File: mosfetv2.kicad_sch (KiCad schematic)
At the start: 26 parts

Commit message: thermal calculations done and Shunt Resistors changed. Not 3, just 2 resistors can dissipate the power.
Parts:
- removed Rsense_A?, Rsense_B?, Rsense_C?: 3mohm, CSNL2512FT3L00:RESC6331X75N, symbol CSNL2512FT3L00:CSNL2512FT3L00
- Rsense_A4: renamed from Rsense_A?; value 3mohm -> 2mohm; footprint CSNL2512FT3L00:RESC6331X75N -> CRF2512-FZ-R002ELF:RESC6432X80N
- Rsense_A5: renamed from Rsense_A?; value 3mohm -> 2mohm
- Rsense_B4, Rsense_B5: renamed from Rsense_B?; value 3mohm -> 2mohm; footprint CSNL2512FT3L00:RESC6331X75N -> CRF2512-FZ-R002ELF:RESC6432X80N
- Rsense_C4, Rsense_C5: renamed from Rsense_C?; value 3mohm -> 2mohm; footprint CSNL2512FT3L00:RESC6331X75N -> CRF2512-FZ-R002ELF:RESC6432X80N
- gave numbers to parts that had none: 17
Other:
- note added: "1.5"
- note added: "Bu değeri biraza daha düşürebiliriz thermal vialar ile"
- note added: "Daha yüksek akımlarla çalışabilmek için soğutma işini güçlendirmek gereklidir!"
- note added: "I = 20A RDSON = 0.005 OHM PLOSS = I^2 * R PLOSS = 2 W ----- RDSON(T=125) = 1.5*0.005 = 0.0075 OHM PLOSS = 3 W ----- MOSFET TEMPERATURE = 25 + 3 * 31.3 = 118.9 C"
- note added: "Sense resistor's power dissipation calculated as: Pmax = Imax^2 * R Pmax = 60^2 * 0.001 Pmax = 3.6 W. So We can use 2 2W resistors. Also we can not achive 60 Amps already."
- note added: "Sense resistor's voltage drop calculated as: Vs = Imax * R Vs = 60 * R (Imax from datasheet, 66A -> 60A) V_SOX: DRV8323 current sense output pin voltage Gain = 40 (Gain selected maximum bcs of power dissipation on shunt resistors) R = 0.001 OHM Vs = 60 * 0.001 = 0.060 V V_SOX = Vs * Gain (Gain = 5/10/20/40) V_SOX = 0.060 *40 = 2.4 V 2.4 V -> 60A -> 3000 (ADC raw) 3.3 V -> 82.5A -> 4095 (ADC raw) 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"
- note added: "Termal Hesaplamalar"
- note added: "WORKING CONDITIONS CONSIDERED AS: I = 20 A T = 120 C Because of thermal cooling limitations"
- note added: "f(I) = T y = I^2*0.0075*31.3+25 y = 0.23475 * I^2 + 25"
- note added: "https://jrainimo.com/build/2024/11/oss-thermal-simulation-of-pcbs/ Açık kaynaklı programları kullanarak sıcaklık analizi yapılabilir."

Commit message: Footprints prepared, first pcb project created.
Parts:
- C29, C31: footprint ul_80ZLJ680MGC18X25:CAP_YX_18X25_RUB -> ul_80ZLJ680MGC18X25:80ZLJ680MGC18X25
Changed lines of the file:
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@@
 			)
 		)
-		(property "Footprint" "ul_80ZLJ680MGC18X25:CAP_YX_18X25_RUB"
+		(property "Footprint" "ul_80ZLJ680MGC18X25:80ZLJ680MGC18X25"
 			(at 265.43 33.02 0)
 			(effects
@@
 			)
 		)
-		(property "Footprint" "ul_80ZLJ680MGC18X25:CAP_YX_18X25_RUB"
+		(property "Footprint" "ul_80ZLJ680MGC18X25:80ZLJ680MGC18X25"
 			(at 238.76 34.29 0)
 			(effects

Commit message: component list updated, all footprints updated and now they are compatible to produce with hand (no 0402 size)
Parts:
- Q10, Q11, Q12, Q8, Q9: footprint STL90N6F7 -> STL90N6F7:STL90N6F7
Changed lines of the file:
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@@
 			)
 		)
-		(property "Footprint" "STL90N6F7"
+		(property "Footprint" "STL90N6F7:STL90N6F7"
 			(at 166.37 186.36 0)
 			(effects
@@
 			)
 		)
-		(property "Footprint" "STL90N6F7"
+		(property "Footprint" "STL90N6F7:STL90N6F7"
 			(at 109.22 186.36 0)
 			(effects
@@
 			)
 		)
-		(property "Footprint" "STL90N6F7"
+		(property "Footprint" "STL90N6F7:STL90N6F7"
 			(at 224.79 186.36 0)
 			(effects
@@
 			)
 		)
-		(property "Footprint" "STL90N6F7"
+		(property "Footprint" "STL90N6F7:STL90N6F7"
 			(at 224.79 158.42 0)
 			(effects
@@
 			)
 		)
-		(property "Footprint" "STL90N6F7"
+		(property "Footprint" "STL90N6F7:STL90N6F7"
 			(at 166.37 158.42 0)
 			(effects

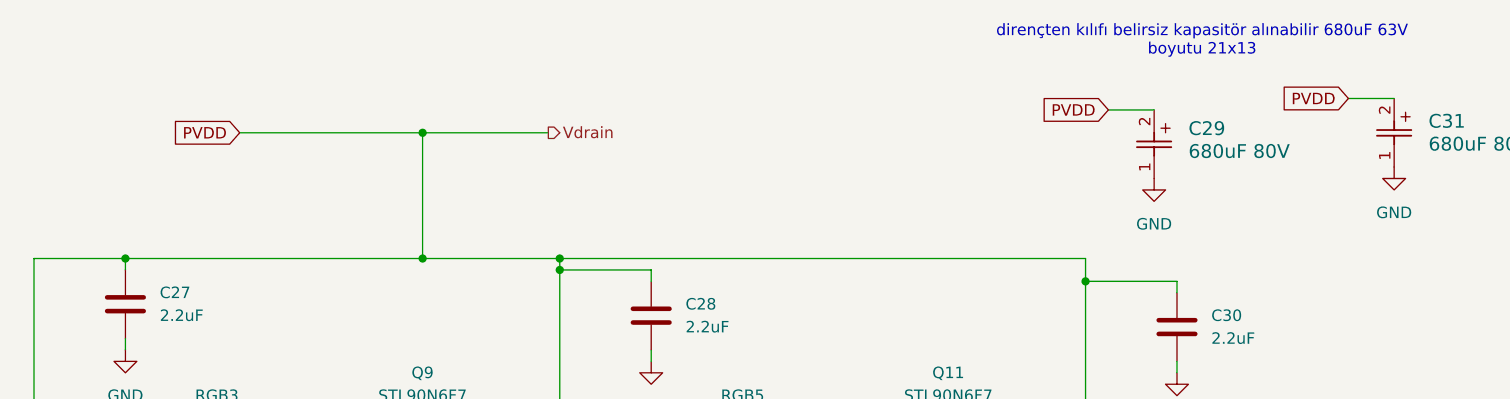
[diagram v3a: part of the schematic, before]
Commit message: some tags chaneged, pcb thinked about pcb component placement, aluminum mosfet carrier pcb and paralelling mosfets
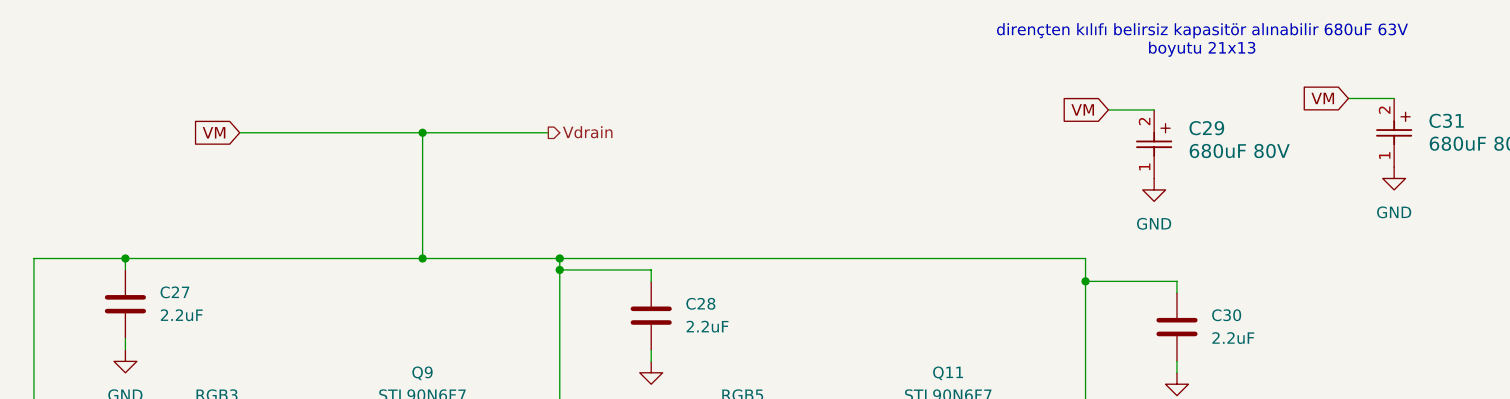
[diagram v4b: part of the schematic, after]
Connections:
- net PVDD renamed VM
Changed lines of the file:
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@@
 		)
 	)
-	(global_label "PVDD"
+	(global_label "VM"
 		(shape input)
 		(at 260.35 25.4 180)
@@
 		)
 	)
-	(global_label "PVDD"
+	(global_label "VM"
 		(shape input)
 		(at 233.68 26.67 180)
@@
 		)
 	)
-	(global_label "PVDD"
+	(global_label "VM"
 		(shape input)
 		(at 137.16 29.21 180)

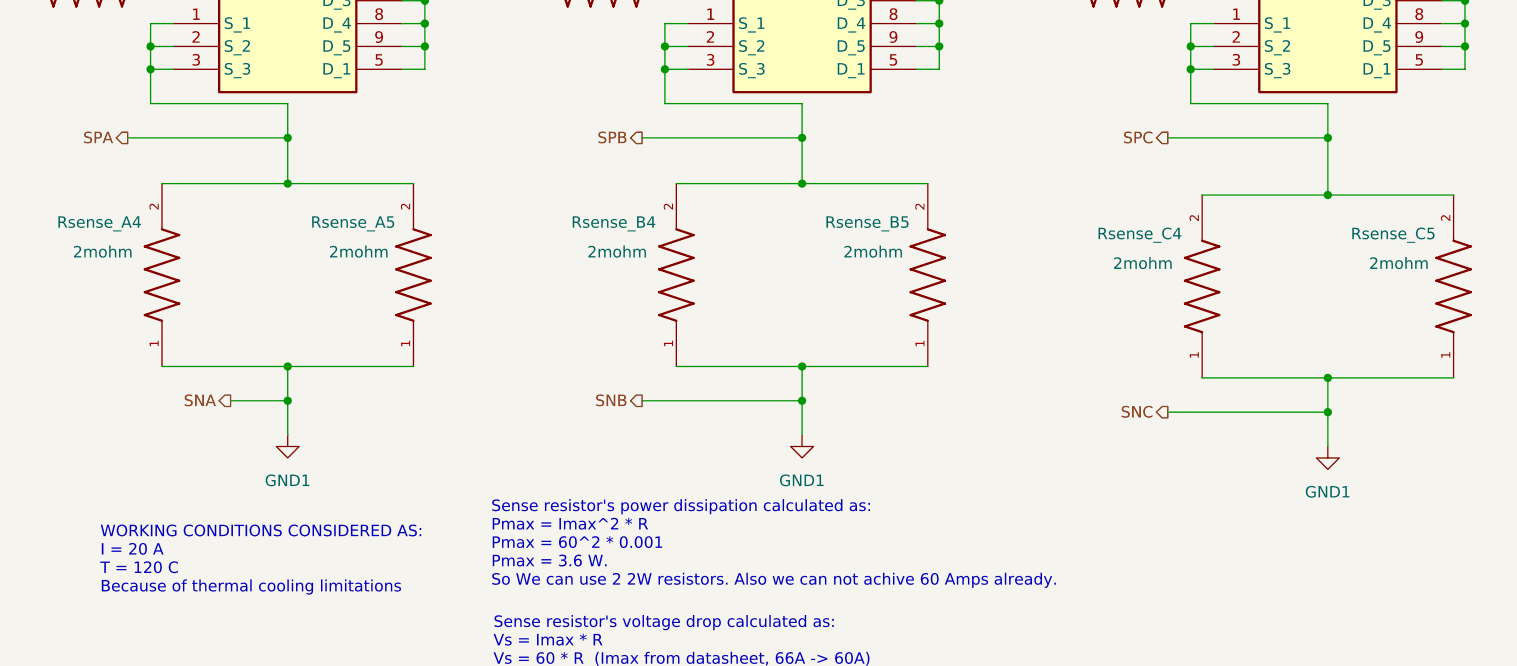
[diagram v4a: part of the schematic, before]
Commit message: started to pcb design, mosfets,shunts drv8323 placement.
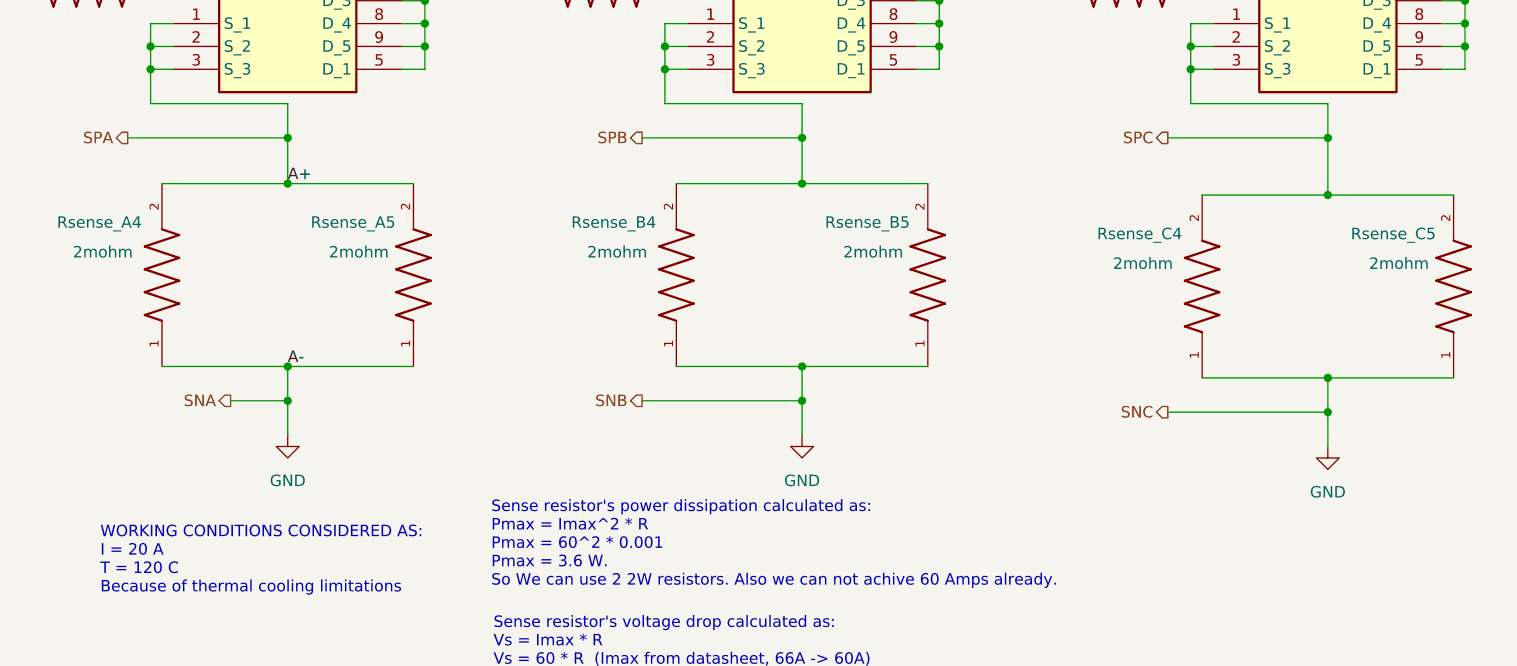
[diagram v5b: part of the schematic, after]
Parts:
- Rsense_A5: footprint CSNL2512FT3L00:RESC6331X75N -> CRF2512-FZ-R002ELF:RESC6432X80N
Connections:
- net GND1 is gone; now on net GND: Rsense_A4.1, Rsense_A5.1, Rsense_B4.1, Rsense_B5.1, Rsense_C4.1, Rsense_C5.1
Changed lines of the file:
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@@
 	(wire
 		(pts
+			(xy 100.33 114.3) (xy 86.36 114.3)
+		)
+		(stroke
+			(width 0)
+			(type default)
+		)
+	)
+	(wire
+		(pts
 			(xy 115.57 91.44) (xy 115.57 93.98)
 		)
@@
 	(wire
 		(pts
-			(xy 86.36 114.3) (xy 100.33 114.3)
-		)
-		(stroke
-			(width 0)
-			(type default)
-		)
-	)
-	(wire
-		(pts
 			(xy 215.9 80.01) (xy 215.9 85.09)
 		)
@@
 		)
 	)
+	(label "A-"
+		(at 100.33 134.62 0)
+		(effects
+			(font
+				(size 1.27 1.27)
+			)
+			(justify left bottom)
+		)
+	)
+	(label "A+"
+		(at 100.33 114.3 0)
+		(effects
+			(font
+				(size 1.27 1.27)
+			)
+			(justify left bottom)
+		)
+	)
 	(global_label "VM"
 		(shape input)
@@
 			)
 		)
-		(property "Value" "GND1"
+		(property "Value" "GND"
 			(at 157.48 147.32 0)
 			(effects
@@
 			)
 		)
-		(property "Footprint" "CSNL2512FT3L00:RESC6331X75N"
+		(property "Footprint" "CRF2512-FZ-R002ELF:RESC6432X80N"
 			(at 114.3 124.46 0)
 			(effects
@@
 			)
 		)
-		(property "Value" "GND1"
+		(property "Value" "GND"
 			(at 215.9 148.59 0)
 			(effects
@@
 			)
 		)
-		(property "Value" "GND1"
+		(property "Value" "GND"
 			(at 100.33 147.32 0)
 			(effects

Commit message: new pcb
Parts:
- C27, C28, C30: footprint Capacitor_SMD:C_0805_2012Metric_Pad1.18x1.45mm_HandSolder -> Capacitor_SMD:C_1206_3216Metric_Pad1.33x1.80mm_HandSolder
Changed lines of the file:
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@@
 			)
 		)
-		(property "Footprint" "Capacitor_SMD:C_0805_2012Metric_Pad1.18x1.45mm_HandSolder"
+		(property "Footprint" "Capacitor_SMD:C_1206_3216Metric_Pad1.33x1.80mm_HandSolder"
 			(at 125.4252 52.07 0)
 			(effects
@@
 			)
 		)
-		(property "Footprint" "Capacitor_SMD:C_0805_2012Metric_Pad1.18x1.45mm_HandSolder"
+		(property "Footprint" "Capacitor_SMD:C_1206_3216Metric_Pad1.33x1.80mm_HandSolder"
 			(at 183.8452 53.34 0)
 			(effects
@@
 			)
 		)
-		(property "Footprint" "Capacitor_SMD:C_0805_2012Metric_Pad1.18x1.45mm_HandSolder"
+		(property "Footprint" "Capacitor_SMD:C_1206_3216Metric_Pad1.33x1.80mm_HandSolder"
 			(at 242.2652 54.61 0)
 			(effects

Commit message: all nıght 4/12
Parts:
- added Batt+1, GND1: power_pad_smd, Pads:Power_pad_smd, symbol Power_Pad_smd:power_pad_smd
- Q10, Q11, Q12, Q7, Q8, Q9: footprint STL90N6F7:STL90N6F7 -> STL90N6F7:STL90N6F7_Thermal_Vias
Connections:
- net GND: now also GND1.1; no longer C27.2, Rsense_A4.1, Rsense_A5.1
- net VM: now also Batt+1.1
- new net PGND: C27.2, Rsense_A4.1, Rsense_A5.1
